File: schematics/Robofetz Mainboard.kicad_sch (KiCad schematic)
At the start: 10 parts, among them J1 On/Off Switch, J2 Battery Connector, J3 Conn_01x04_Pin, J4 Motor 1, J5 Motor 2, J6 Weapon Controller, U1 ESP32, U2 DCDC, U3 ROB-14450

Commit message: Added libraries
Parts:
- added U4: ESP32-C5-DevKitC-1, PCM_Espressif:ESP32-C5-DevKitC-1, symbol Espressif:ESP32-C5-DevKitC-1
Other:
- note added: "ESP32 low level control (option 1)"
- note added: "ESP32 low level control (option 2)"
- note removed: "ESP32 low level control"
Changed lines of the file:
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@@
 	)
 	(rectangle
+		(start 19.05 130.81)
+		(end 163.83 193.04)
+		(stroke
+			(width 0)
+			(type dash)
+			(color 97 95 24 1)
+		)
+		(fill
+			(type none)
+		)
+	)
+	(rectangle
 		(start 12.7 99.06)
 		(end 73.66 127.635)
@@
 		)
 	)
+	(text "ESP32 low level control (option 2)\n\n"
+		(exclude_from_sim no)
+		(at 90.17 136.652 0)
+		(effects
+			(font
+				(size 2 2)
+				(thickness 0.4)
+				(bold yes)
+			)
+		)
+	)
 	(text "Motor Supply +"
 		(exclude_from_sim no)
@@
 		)
 	)
-	(text "ESP32 low level control\n"
+	(text "ESP32 low level control (option 1)\n"
 		(exclude_from_sim no)
 		(at 145.796 39.37 0)
@@
 			)
 		)
+	)
+	(symbol
+		(lib_id "Espressif:ESP32-C5-DevKitC-1")
+		(at 87.63 143.51 0)
+		(unit 1)
+		(exclude_from_sim no)
+		(in_bom yes)
+		(on_board yes)
+		(dnp no)
+		(fields_autoplaced yes)
+		(property "Reference" "U4"
+			(at 87.63 139.7 0)
+			(effects
+				(font
+					(size 1.27 1.27)
+				)
+			)
+		)
+		(property "Value" "ESP32-C5-DevKitC-1"
+			(at 87.63 142.24 0)
+			(effects
+				(font
+					(size 1.27 1.27)
+				)
+			)
+		)
+		(property "Footprint" "PCM_Espressif:ESP32-C5-DevKitC-1"
+			(at 86.614 194.818 0)
+			(effects
+				(font
+					(size 1.27 1.27)
+				)
+				(hide yes)
+			)
+		)
+		(property "Datasheet" "https://docs.espressif.com/projects/esp-dev-kits/en/latest/esp32c5/esp32-c5-devkitc-1/user_guide.html"
+			(at 87.63 144.78 0)
+			(effects
+				(font
+					(size 1.27 1.27)
+				)
+			)
+		)
+		(property "Description" ""
+			(at 87.63 143.51 0)
+			(effects
+				(font
+					(size 1.27 1.27)
+				)
+				(hide yes)
+			)
+		)
+		(pin "17"
+		)
+		(pin "29"
+		)
+		(pin "25"
+		)
+		(pin "16"
+		)
+		(pin "20"
+		)
+		(pin "32"
+		)
+		(pin "6"
+		)
+		(pin "24"
+		)
+		(pin "19"
+		)
+		(pin "12"
+		)
+		(pin "11"
+		)
+		(pin "21"
+		)
+		(pin "18"
+		)
+		(pin "22"
+		)
+		(pin "10"
+		)
+		(pin "13"
+		)
+		(pin "15"
+		)
+		(pin "7"
+		)
+		(pin "8"
+		)
+		(pin "3"
+		)
+		(pin "2"
+		)
+		(pin "14"
+		)
+		(pin "1"
+		)
+		(pin "4"
+		)
+		(pin "5"
+		)
+		(pin "26"
+		)
+		(pin "31"
+		)
+		(pin "23"
+		)
+		(pin "27"
+		)
+		(pin "30"
+		)
+		(pin "28"
+		)
+		(pin "9"
+		)
+		(instances
+			(project ""
+				(path "/bf47f329-3b1a-4bcb-94ac-b8898ea14cde"
+					(reference "U4")
+					(unit 1)
+				)
+			)
+		)

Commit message: Updated libararies, passed ERC
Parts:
- removed U1: ESP32, ESP32_devboard:buck_converter_robofetz, symbol ESP32_devboard:ESP32_devboard
- removed U4: ESP32-C5-DevKitC-1, PCM_Espressif:ESP32-C5-DevKitC-1, symbol Espressif:ESP32-C5-DevKitC-1
- U3: footprint ROB-14450:MODULE_ROB-14450 -> ROB-14450:ROB14450
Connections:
- net GND: now also J4.5 (Pin_5), J5.5 (Pin_5), J6.1 (Pin_1), U2.4 (OUT-)
- net Supply 16V: now also J1.1 (Pin_1), J2.1 (Pin_1), J6.3 (Pin_3), U3.1 (VM)
- net Supply 3.3V: now also J4.2 (Pin_2), J5.2 (Pin_2), U3.2 (VCC)
- net at J2.2 (Pin_2): now also J3.4 (Pin_4)
- net at U2.1 (IN+): now also D1.1 (K)
- net at U2.2 (IN-): now also J3.1 (Pin_1)
- net Supply 5V: now reaches U2.3 (OUT+)
- net at J1.2 (Pin_2): now also J3.3 (Pin_3)
- net at J3.2 (Pin_2): now also D1.2 (A)
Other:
- added sheet Microcontrollers (microcontrollers.kicad_sch)
- note added: "ESP32 high level logic"
- note removed: "ESP32 low level control (option 1)"
- note removed: "ESP32 low level control (option 2)"
- moved on the sheet: D1, J1, J2, J3, J6, U2

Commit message: Finished PCB Version 1
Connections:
- net Supply 16V is gone; now on net +15V: J1.1 (Pin_1), J2.1 (Pin_1), J6.3 (Pin_3), U3.1 (VM)
- net GND: now also J2.2 (Pin_2), J3.1 (Pin_1), J3.4 (Pin_4), U2.2 (IN-)
- net +15V: now reaches D1.1 (K), U2.1 (IN+)
- net +15V: now also J1.2 (Pin_2), J3.3 (Pin_3)
- net Supply 5V renamed +5V

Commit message: updated schematics + pcb layout
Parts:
- added R1, R2: R, Resistor_THT:R_Axial_DIN0204_L3.6mm_D1.6mm_P1.90mm_Vertical, symbol Device:R
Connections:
- net Supply 3.3V: now also J6.3 (Pin_3), R2.1
- net WPN Control: now also R1.1; no longer J6.2 (Pin_2)
- removed net +15V: D1.1 (K), J1.1 (Pin_1), J1.2 (Pin_2), J2.1 (Pin_1), J3.3 (Pin_3), J6.3 (Pin_3), U2.1 (IN+), U3.1 (VM)
- new net: J1.1 (Pin_1), J2.1 (Pin_1)
- new net: D1.1 (K), U2.1 (IN+)
- new net: J6.2 (Pin_2), R1.2, R2.2
- new net Supply 16V: J1.2 (Pin_2), J3.3 (Pin_3), U3.1 (VM)
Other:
- note added: "Network connection"
- moved on the sheet: J6

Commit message: updated schematics + layout
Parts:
- removed J1: On/Off Switch, Connector_JST:JST_EH_B2B-EH-A_1x02_P2.50mm_Vertical, symbol Connector:Conn_01x02_Pin
- removed J3: Conn_01x04_Pin, Connector_JST:JST_EH_B4B-EH-A_1x04_P2.50mm_Vertical, symbol Connector:Conn_01x04_Pin
- added J7: Conn_01x04_Pin, symbol Connector:Conn_01x04_Pin
- J2: value Battery Connector -> PCB Power Connector
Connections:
- net +5V: now also J7.2 (Pin_2), J7.3 (Pin_3)
- net GND: now also J7.4 (Pin_4)
- net Supply 16V: now also J2.1 (Pin_1), U2.1 (IN+)
- net Supply 5V ESP: now reaches D1.1 (K)
- net Supply 5V ESP: no longer U2.1 (IN+)
- net at D1.2 (A): now also J7.1 (Pin_1)
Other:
- note added: "5V"
- note added: "ESP supply"
- note added: "GND"
- note removed: "IN+"
- note removed: "IN-"
- note removed: "OUT+"
- note removed: "OUT-"
- moved on the sheet: D1

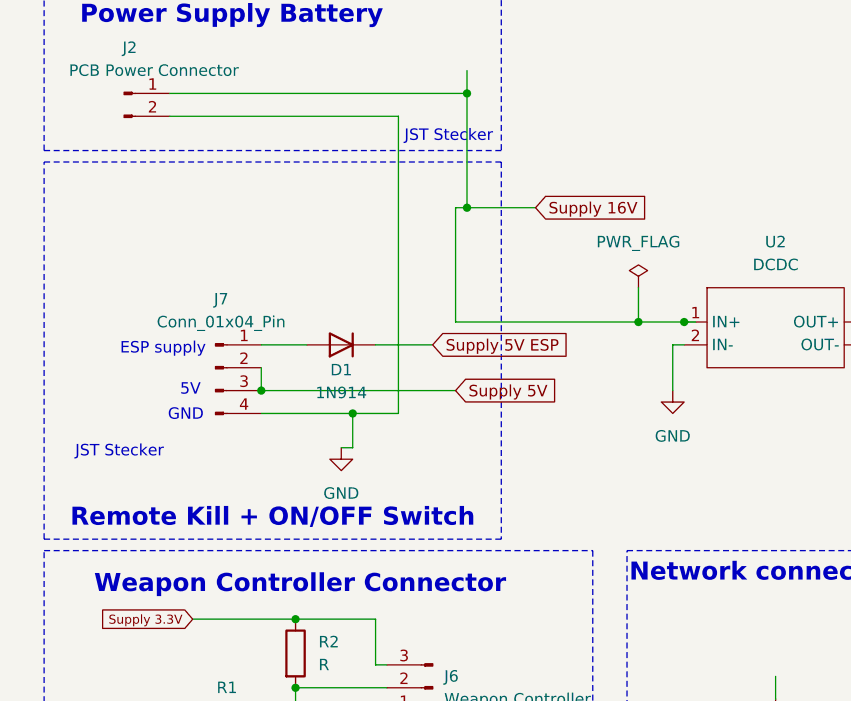
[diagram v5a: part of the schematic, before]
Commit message: updated layout
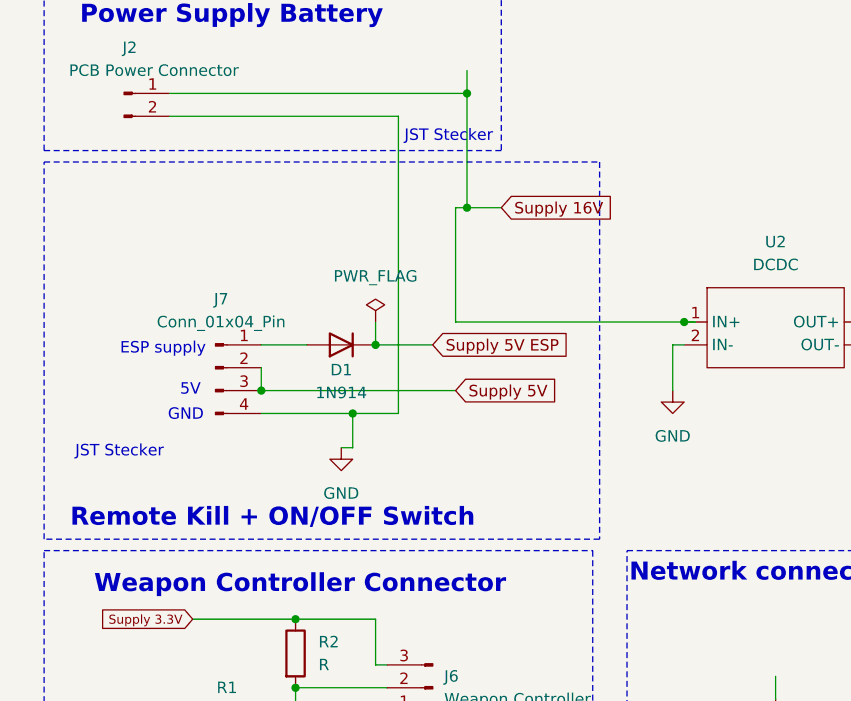
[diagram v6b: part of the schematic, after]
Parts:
- J7: footprint (none) -> Connector_JST:JST_EH_B4B-EH-A_1x04_P2.50mm_Vertical
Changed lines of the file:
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@@
 	(rectangle
 		(start 22.86 57.15)
-		(end 73.66 99.06)
+		(end 84.582 99.06)
 		(stroke
 			(width 0)
@@
 	)
 	(junction
-		(at 88.9 74.93)
-		(diameter 0)
-		(color 0 0 0 0)
-	)
-	(junction
 		(at 256.54 66.04)
 		(diameter 0)
@@
 		(color 0 0 0 0)
 	)
+	(junction
+		(at 59.69 77.47)
+		(diameter 0)
+		(color 0 0 0 0)
+	)
 	(wire
 		(pts
@@
 	(wire
 		(pts
-			(xy 88.9 74.93) (xy 68.58 74.93)
-		)
-		(stroke
-			(width 0)
-			(type default)
-		)
-	)
-	(wire
-		(pts
 			(xy 62.23 52.07) (xy 62.23 85.09)
 		)
@@
 	(wire
 		(pts
-			(xy 88.9 74.93) (xy 93.98 74.93)
+			(xy 68.58 74.93) (xy 93.98 74.93)
 		)
 		(stroke
@@
 	(wire
 		(pts
-			(xy 46.99 77.47) (xy 52.07 77.47)
+			(xy 59.69 74.93) (xy 59.69 77.47)
 		)
 		(stroke
@@
 	(wire
 		(pts
-			(xy 120.65 71.12) (xy 120.65 72.39)
+			(xy 46.99 77.47) (xy 52.07 77.47)
 		)
 		(stroke
@@
 	(wire
 		(pts
-			(xy 57.15 88.9) (xy 55.88 88.9)
+			(xy 120.65 71.12) (xy 120.65 72.39)
 		)
 		(stroke
@@
 	(wire
 		(pts
-			(xy 59.69 107.95) (xy 59.69 113.03)
+			(xy 57.15 88.9) (xy 55.88 88.9)
 		)
 		(stroke
@@
 	(wire
 		(pts
-			(xy 120.65 72.39) (xy 116.84 72.39)
+			(xy 59.69 107.95) (xy 59.69 113.03)
 		)
 		(stroke
@@
 	(wire
 		(pts
-			(xy 36.83 52.07) (xy 62.23 52.07)
+			(xy 120.65 72.39) (xy 116.84 72.39)
 		)
 		(stroke
@@
 	(wire
 		(pts
-			(xy 88.9 71.12) (xy 88.9 74.93)
+			(xy 36.83 52.07) (xy 62.23 52.07)
 		)
 		(stroke
@@
 	(wire
 		(pts
-			(xy 69.85 62.23) (xy 77.47 62.23)
+			(xy 69.85 62.23) (xy 73.66 62.23)
 		)
 		(stroke
@@
 	(global_label "Supply 16V"
 		(shape input)
-		(at 77.47 62.23 0)
+		(at 73.66 62.23 0)
 		(fields_autoplaced yes)
 		(effects
@@
 		)
 		(property "Intersheetrefs" "${INTERSHEET_REFS}"
-			(at 91.2197 62.23 0)
+			(at 87.4097 62.23 0)
 			(effects
 				(font
@@
 	)
 	(symbol
-		(lib_id "power:PWR_FLAG")
-		(at 88.9 71.12 0)
-		(unit 1)
-		(exclude_from_sim no)
-		(in_bom yes)
-		(on_board yes)
-		(dnp no)
-		(fields_autoplaced yes)
-		(property "Reference" "#FLG01"
-			(at 88.9 69.215 0)
-			(effects
-				(font
-					(size 1.27 1.27)
-				)
-				(hide yes)
-			)
-		)
-		(property "Value" "PWR_FLAG"
-			(at 88.9 66.04 0)
-			(effects
-				(font
-					(size 1.27 1.27)
-				)
-			)
-		)
-		(property "Footprint" ""
-			(at 88.9 71.12 0)
-			(effects
-				(font
-					(size 1.27 1.27)
-				)
-				(hide yes)
-			)
-		)
-		(property "Datasheet" "~"
-			(at 88.9 71.12 0)
-			(effects
-				(font
-					(size 1.27 1.27)
-				)
-				(hide yes)
-			)
-		)
-		(property "Description" "Special symbol for telling ERC where power comes from"
-			(at 88.9 71.12 0)
-			(effects
-				(font
-					(size 1.27 1.27)
-				)
-				(hide yes)
-			)
-		)
-		(pin "1"
-		)
-		(instances
-			(project ""
-				(path "/bf47f329-3b1a-4bcb-94ac-b8898ea14cde"
-					(reference "#FLG01")
-					(unit 1)
-				)
-			)
-		)
-	)
-	(symbol
 		(lib_id "Connector:Conn_01x04_Pin")
 		(at 41.91 80.01 0)
@@
 			)
 		)
-		(property "Footprint" ""
+		(property "Footprint" "Connector_JST:JST_EH_B4B-EH-A_1x04_P2.50mm_Vertical"
 			(at 41.91 80.01 0)
 			(effects
@@
 					(unit 1)
 				)
+			)
+		)
+	)
+	(symbol
+		(lib_id "power:PWR_FLAG")
+		(at 59.69 74.93 0)
+		(unit 1)
+		(exclude_from_sim no)
+		(in_bom yes)
+		(on_board yes)
+		(dnp no)
+		(fields_autoplaced yes)
+		(property "Reference" "#FLG01"
+			(at 59.69 73.025 0)
+			(effects
+				(font
+					(size 1.27 1.27)
+				)
+				(hide yes)
+			)
+		)
+		(property "Value" "PWR_FLAG"
+			(at 59.69 69.85 0)
+			(effects
+				(font
+					(size 1.27 1.27)
+				)
+			)
+		)
+		(property "Footprint" ""
+			(at 59.69 74.93 0)
+			(effects
+				(font
+					(size 1.27 1.27)
+				)
+				(hide yes)
+			)
+		)
+		(property "Datasheet" "~"
+			(at 59.69 74.93 0)
+			(effects
+				(font
+					(size 1.27 1.27)
+				)
+				(hide yes)
+			)
+		)
+		(property "Description" "Special symbol for telling ERC where power comes from"
+			(at 59.69 74.93 0)
+			(effects
+				(font
+					(size 1.27 1.27)
+				)
+				(hide yes)
+			)
+		)
+		(pin "1"
+		)
+		(instances
+			(project ""
+				(path "/bf47f329-3b1a-4bcb-94ac-b8898ea14cde"
+					(reference "#FLG01")
+					(unit 1)
+				)
